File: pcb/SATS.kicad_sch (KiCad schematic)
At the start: 34 parts, among them J1 Raspberry_Pi_2_3, J10 EXT_GPIO, J11 EXT_GPIO, J12 EXT_GPIO, J13 EXT_GPIO, J2 A00-432-262-450, J3 AudioJack4_SwitchTR1, J4 5V, J5 3.3V, J6 Card LED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

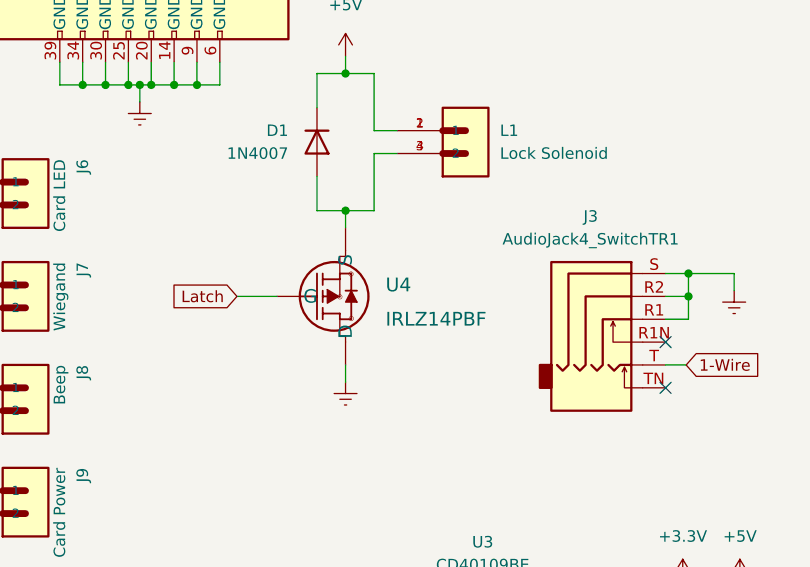
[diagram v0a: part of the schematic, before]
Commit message: Add Grounded Copper Fills to Row Breakout and Main Board
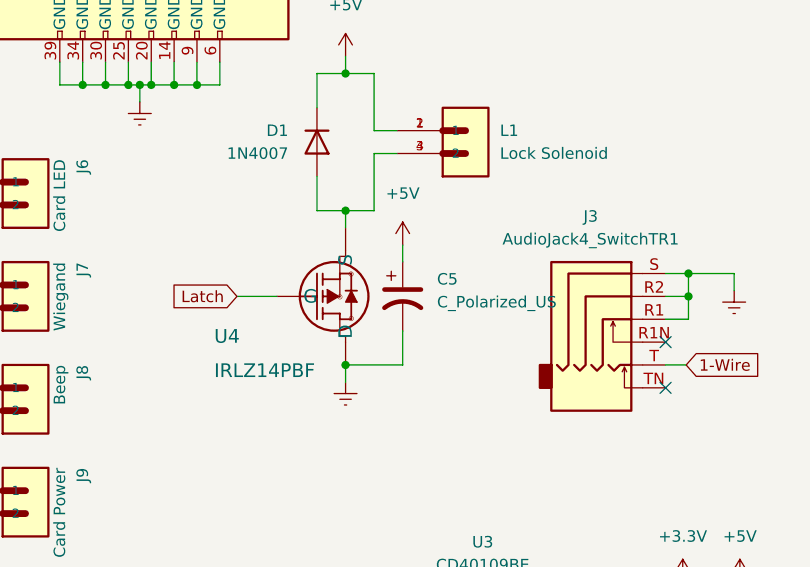
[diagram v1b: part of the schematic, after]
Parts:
- added C5: C_Polarized_US, symbol Device:C_Polarized_US
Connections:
- net +5V: now also C5.1
- net Earth: now also C5.2
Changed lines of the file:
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@@
   (junction (at 57.15 172.085) (diameter 0) (color 0 0 0 0)
   )
+  (junction (at 77.47 124.46) (diameter 0) (color 0 0 0 0)
+  )
   (junction (at 50.8 93.345) (diameter 0) (color 0 0 0 0)
   )
@@
     (stroke (width 0) (type default) (color 0 0 0 0))
   )
+  (wire (pts (xy 83.82 111.125) (xy 83.82 113.03))
+    (stroke (width 0) (type default) (color 0 0 0 0))
+  )
   (wire (pts (xy 83.185 98.425) (xy 80.645 98.425))
     (stroke (width 0) (type default) (color 0 0 0 0))
@@
     (stroke (width 0) (type default) (color 0 0 0 0))
   )
+  (wire (pts (xy 83.82 120.65) (xy 83.82 124.46))
+    (stroke (width 0) (type default) (color 0 0 0 0))
+  )
   (wire (pts (xy 50.8 21.59) (xy 50.8 24.765))
     (stroke (width 0) (type default) (color 0 0 0 0))
@@
     (stroke (width 0) (type default) (color 0 0 0 0))
   )
+  (wire (pts (xy 83.82 124.46) (xy 77.47 124.46))
+    (stroke (width 0) (type default) (color 0 0 0 0))
+  )
   (wire (pts (xy 58.42 93.345) (xy 55.88 93.345))
     (stroke (width 0) (type default) (color 0 0 0 0))
@@
     (pin "1")
   )
+  (symbol (lib_id "Device:C_Polarized_US") (at 83.82 116.84 0) (unit 1)
+    (in_bom yes) (on_board yes) (fields_autoplaced)
+    (property "Reference" "C5" (id 0) (at 87.63 114.9349 0)
+      (effects (font (size 1.27 1.27)) (justify left))
+    )
+    (property "Value" "C_Polarized_US" (id 1) (at 87.63 117.4749 0)
+      (effects (font (size 1.27 1.27)) (justify left))
+    )
+    (property "Footprint" "" (id 2) (at 83.82 116.84 0)
+      (effects (font (size 1.27 1.27)) hide)
+    )
+    (property "Datasheet" "~" (id 3) (at 83.82 116.84 0)
+      (effects (font (size 1.27 1.27)) hide)
+    )
+    (pin "1")
+    (pin "2")
+  )
   (symbol (lib_id "power:+3.3V") (at 57.15 168.275 0) (unit 1)
     (in_bom yes) (on_board yes)
@@
   )
   (symbol (lib_id "IRLZ14PBF:IRLZ14PBF") (at 69.85 116.84 0) (unit 1)
-    (in_bom yes) (on_board yes) (fields_autoplaced)
-    (property "Reference" "U4" (id 0) (at 81.915 115.57 0)
+    (in_bom yes) (on_board yes)
+    (property "Reference" "U4" (id 0) (at 62.865 121.285 0)
       (effects (font (size 1.524 1.524)) (justify left))
     )
-    (property "Value" "IRLZ14PBF" (id 1) (at 81.915 119.38 0)
+    (property "Value" "IRLZ14PBF" (id 1) (at 62.865 125.095 0)
       (effects (font (size 1.524 1.524)) (justify left))
     )
@@
     (pin "4")
   )
+  (symbol (lib_id "power:+5V") (at 83.82 111.125 0) (unit 1)
+    (in_bom yes) (on_board yes) (fields_autoplaced)
+    (property "Reference" "#PWR?" (id 0) (at 83.82 114.935 0)
+      (effects (font (size 1.27 1.27)) hide)
+    )
+    (property "Value" "+5V" (id 1) (at 83.82 105.41 0))
+    (property "Footprint" "" (id 2) (at 83.82 111.125 0)
+      (effects (font (size 1.27 1.27)) hide)
+    )
+    (property "Datasheet" "" (id 3) (at 83.82 111.125 0)
+      (effects (font (size 1.27 1.27)) hide)
+    )
+    (pin "1")
+  )
   (symbol (lib_id "power:+5V") (at 107.315 31.115 0) (mirror x) (unit 1)
     (in_bom yes) (on_board yes) (fields_autoplaced)
@@
       (reference "#PWR0141") (unit 1) (value "Earth") (footprint "")
     )
+    (path "/b2205868-ea15-4ad8-be8d-37b937090977"
+      (reference "#PWR?") (unit 1) (value "+5V") (footprint "")
+    )
     (path "/76312551-1f93-4c3b-b646-01a8c308431a"
       (reference "C1") (unit 1) (value "100nF") (footprint "Capacitor_THT:C_Rect_L7.0mm_W3.5mm_P5.00mm")
@@
       (reference "C4") (unit 1) (value "100nF") (footprint "Capacitor_THT:C_Rect_L7.0mm_W3.5mm_P5.00mm")
     )
+    (path "/48997d22-8d2f-4e8f-9ecb-f994183fe17f"
+      (reference "C5") (unit 1) (value "C_Polarized_US") (footprint "")
+    )
     (path "/10ba1107-77c4-4d57-9ffa-56a66acd4eae"

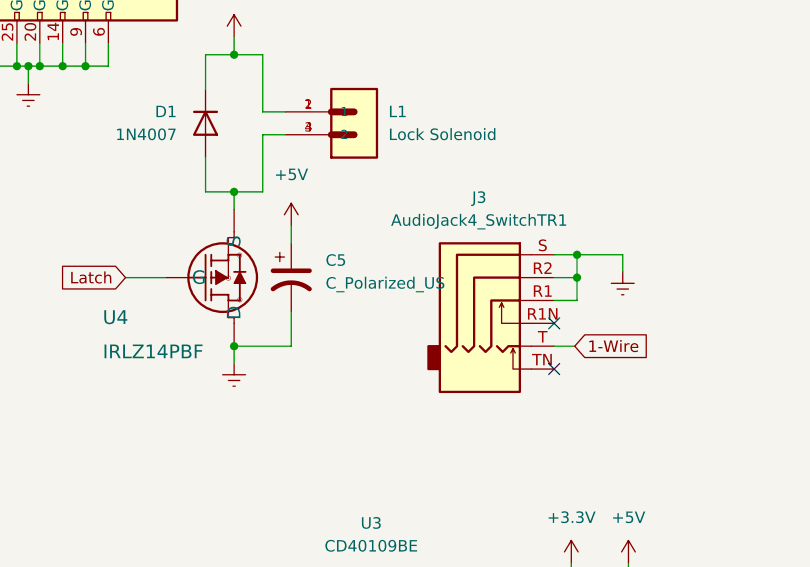
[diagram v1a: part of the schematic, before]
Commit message: Add power cap for Latch
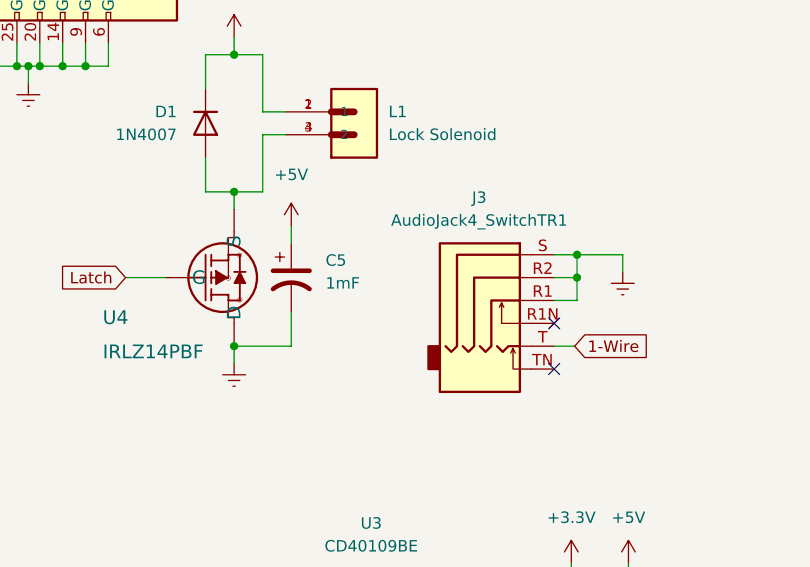
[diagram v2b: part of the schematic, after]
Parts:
- C5: value C_Polarized_US -> 1mF; footprint (none) -> Capacitor_THT:CP_Radial_D10.0mm_P5.00mm
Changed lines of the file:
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@@
       (effects (font (size 1.27 1.27)) (justify left))
     )
-    (property "Value" "C_Polarized_US" (id 1) (at 87.63 117.4749 0)
-      (effects (font (size 1.27 1.27)) (justify left))
-    )
-    (property "Footprint" "" (id 2) (at 83.82 116.84 0)
+    (property "Value" "1mF" (id 1) (at 87.63 117.4749 0)
+      (effects (font (size 1.27 1.27)) (justify left))
+    )
+    (property "Footprint" "Capacitor_THT:CP_Radial_D10.0mm_P5.00mm" (id 2) (at 83.82 116.84 0)
       (effects (font (size 1.27 1.27)) hide)
     )
@@
   (symbol (lib_id "power:+5V") (at 83.82 111.125 0) (unit 1)
     (in_bom yes) (on_board yes) (fields_autoplaced)
-    (property "Reference" "#PWR?" (id 0) (at 83.82 114.935 0)
+    (property "Reference" "#PWR0142" (id 0) (at 83.82 114.935 0)
       (effects (font (size 1.27 1.27)) hide)
     )
@@
     )
     (path "/b2205868-ea15-4ad8-be8d-37b937090977"
-      (reference "#PWR?") (unit 1) (value "+5V") (footprint "")
+      (reference "#PWR0142") (unit 1) (value "+5V") (footprint "")
     )
     (path "/76312551-1f93-4c3b-b646-01a8c308431a"
@@
     )
     (path "/48997d22-8d2f-4e8f-9ecb-f994183fe17f"
-      (reference "C5") (unit 1) (value "C_Polarized_US") (footprint "")
+      (reference "C5") (unit 1) (value "1mF") (footprint "Capacitor_THT:CP_Radial_D10.0mm_P5.00mm")
     )
     (path "/10ba1107-77c4-4d57-9ffa-56a66acd4eae"

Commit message: Rev 3 Complete
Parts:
- added R2: 10, Resistor_THT:R_Axial_DIN0207_L6.3mm_D2.5mm_P7.62mm_Horizontal, symbol Device:R_US
- renumbered R4 to R1
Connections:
- net at L1.3 (2), L1.4 (2), U4.3 (S): now also R2.2; no longer D1.2 (A)
- new net: D1.2 (A), R2.1
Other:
- moved on the sheet: C5, U4
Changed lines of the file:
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@@
   (junction (at 57.15 172.085) (diameter 0) (color 0 0 0 0)
   )
-  (junction (at 77.47 124.46) (diameter 0) (color 0 0 0 0)
+  (junction (at 77.47 133.35) (diameter 0) (color 0 0 0 0)
   )
   (junction (at 50.8 93.345) (diameter 0) (color 0 0 0 0)
   )
-  (junction (at 77.47 107.315) (diameter 0) (color 0 0 0 0)
+  (junction (at 77.47 116.205) (diameter 0) (color 0 0 0 0)
   )
   (junction (at 53.34 93.345) (diameter 0) (color 0 0 0 0)
@@
     (stroke (width 0) (type default) (color 0 0 0 0))
   )
-  (wire (pts (xy 74.295 107.315) (xy 77.47 107.315))
+  (wire (pts (xy 74.295 116.205) (xy 77.47 116.205))
     (stroke (width 0) (type default) (color 0 0 0 0))
   )
@@
     (stroke (width 0) (type default) (color 0 0 0 0))
   )
-  (wire (pts (xy 77.47 107.315) (xy 80.645 107.315))
+  (wire (pts (xy 77.47 116.205) (xy 80.645 116.205))
     (stroke (width 0) (type default) (color 0 0 0 0))
   )
@@
     (stroke (width 0) (type default) (color 0 0 0 0))
   )
+  (wire (pts (xy 74.295 113.665) (xy 74.295 116.205))
+    (stroke (width 0) (type default) (color 0 0 0 0))
+  )
   (wire (pts (xy 73.66 34.925) (xy 77.47 34.925))
     (stroke (width 0) (type default) (color 0 0 0 0))
@@
     (stroke (width 0) (type default) (color 0 0 0 0))
   )
-  (wire (pts (xy 83.82 111.125) (xy 83.82 113.03))
+  (wire (pts (xy 83.82 120.015) (xy 83.82 121.92))
     (stroke (width 0) (type default) (color 0 0 0 0))
   )
@@
     (stroke (width 0) (type default) (color 0 0 0 0))
   )
+  (wire (pts (xy 74.295 103.505) (xy 74.295 106.045))
+    (stroke (width 0) (type default) (color 0 0 0 0))
+  )
   (wire (pts (xy 160.655 133.985) (xy 158.115 133.985))
     (stroke (width 0) (type default) (color 0 0 0 0))
@@
     (stroke (width 0) (type default) (color 0 0 0 0))
   )
-  (wire (pts (xy 77.47 107.315) (xy 77.47 109.22))
+  (wire (pts (xy 77.47 116.205) (xy 77.47 118.11))
     (stroke (width 0) (type default) (color 0 0 0 0))
   )
@@
     (stroke (width 0) (type default) (color 0 0 0 0))
   )
-  (wire (pts (xy 65.405 116.84) (xy 69.85 116.84))
+  (wire (pts (xy 65.405 125.73) (xy 69.85 125.73))
     (stroke (width 0) (type default) (color 0 0 0 0))
   )
@@
     (stroke (width 0) (type default) (color 0 0 0 0))
   )
-  (wire (pts (xy 83.82 120.65) (xy 83.82 124.46))
+  (wire (pts (xy 83.82 129.54) (xy 83.82 133.35))
     (stroke (width 0) (type default) (color 0 0 0 0))
   )
@@
     (stroke (width 0) (type default) (color 0 0 0 0))
   )
-  (wire (pts (xy 83.82 124.46) (xy 77.47 124.46))
+  (wire (pts (xy 83.82 133.35) (xy 77.47 133.35))
     (stroke (width 0) (type default) (color 0 0 0 0))
   )
@@
     (stroke (width 0) (type default) (color 0 0 0 0))
   )
-  (wire (pts (xy 80.645 100.965) (xy 80.645 107.315))
+  (wire (pts (xy 80.645 100.965) (xy 80.645 116.205))
     (stroke (width 0) (type default) (color 0 0 0 0))
   )
@@
     (stroke (width 0) (type default) (color 0 0 0 0))
   )
-  (wire (pts (xy 74.295 103.505) (xy 74.295 107.315))
-    (stroke (width 0) (type default) (color 0 0 0 0))
-  )
-  (wire (pts (xy 77.47 124.46) (xy 77.47 126.365))
+  (wire (pts (xy 77.47 133.35) (xy 77.47 135.255))
     (stroke (width 0) (type default) (color 0 0 0 0))
   )
@@
     )
   )
-  (global_label "Latch" (shape input) (at 65.405 116.84 180) (fields_autoplaced)
+  (global_label "Latch" (shape input) (at 65.405 125.73 180) (fields_autoplaced)
     (effects (font (size 1.27 1.27)) (justify right))
-    (property "Intersheet References" "${INTERSHEET_REFS}" (id 0) (at 57.8514 116.7606 0)
+    (property "Intersheet References" "${INTERSHEET_REFS}" (id 0) (at 57.8514 125.6506 0)
       (effects (font (size 1.27 1.27)) (justify right) hide)
     )
@@
     (pin "1")
   )
-  (symbol (lib_id "power:Earth") (at 77.47 126.365 0) (unit 1)
+  (symbol (lib_id "Device:R_US") (at 74.295 109.855 0) (unit 1)
+    (in_bom yes) (on_board yes)
+    (property "Reference" "R2" (id 0) (at 67.31 108.585 0)
+      (effects (font (size 1.27 1.27)) (justify left))
+    )
+    (property "Value" "10" (id 1) (at 67.31 111.125 0)
+      (effects (font (size 1.27 1.27)) (justify left))
+    )
+    (property "Footprint" "Resistor_THT:R_Axial_DIN0207_L6.3mm_D2.5mm_P7.62mm_Horizontal" (id 2) (at 75.311 110.109 90)
+      (effects (font (size 1.27 1.27)) hide)
+    )
+    (property "Datasheet" "~" (id 3) (at 74.295 109.855 0)
+      (effects (font (size 1.27 1.27)) hide)
+    )
+    (pin "1")
+    (pin "2")
+  )
+  (symbol (lib_id "power:Earth") (at 77.47 135.255 0) (unit 1)
     (in_bom yes) (on_board yes) (fields_autoplaced)
-    (property "Reference" "#PWR0129" (id 0) (at 77.47 132.715 0)
+    (property "Reference" "#PWR0129" (id 0) (at 77.47 141.605 0)
       (effects (font (size 1.27 1.27)) hide)
     )
-    (property "Value" "Earth" (id 1) (at 77.47 130.175 0)
+    (property "Value" "Earth" (id 1) (at 77.47 139.065 0)
       (effects (font (size 1.27 1.27)) hide)
     )
-    (property "Footprint" "" (id 2) (at 77.47 126.365 0)
+    (property "Footprint" "" (id 2) (at 77.47 135.255 0)
       (effects (font (size 1.27 1.27)) hide)
     )
-    (property "Datasheet" "~" (id 3) (at 77.47 126.365 0)
+    (property "Datasheet" "~" (id 3) (at 77.47 135.255 0)
       (effects (font (size 1.27 1.27)) hide)
     )
@@
     (pin "1")
   )
-  (symbol (lib_id "Device:C_Polarized_US") (at 83.82 116.84 0) (unit 1)
+  (symbol (lib_id "Device:C_Polarized_US") (at 83.82 125.73 0) (unit 1)
     (in_bom yes) (on_board yes) (fields_autoplaced)
-    (property "Reference" "C5" (id 0) (at 87.63 114.9349 0)
+    (property "Reference" "C5" (id 0) (at 87.63 123.8249 0)
       (effects (font (size 1.27 1.27)) (justify left))
     )
-    (property "Value" "1mF" (id 1) (at 87.63 117.4749 0)
+    (property "Value" "1mF" (id 1) (at 87.63 126.3649 0)
       (effects (font (size 1.27 1.27)) (justify left))
     )
-    (property "Footprint" "Capacitor_THT:CP_Radial_D10.0mm_P5.00mm" (id 2) (at 83.82 116.84 0)
+    (property "Footprint" "Capacitor_THT:CP_Radial_D10.0mm_P5.00mm" (id 2) (at 83.82 125.73 0)
       (effects (font (size 1.27 1.27)) hide)
     )
-    (property "Datasheet" "~" (id 3) (at 83.82 116.84 0)
+    (property "Datasheet" "~" (id 3) (at 83.82 125.73 0)
       (effects (font (size 1.27 1.27)) hide)
     )
@@
   (symbol (lib_id "Device:R_US") (at 95.25 66.675 180) (unit 1)
     (in_bom yes) (on_board yes) (fields_autoplaced)
-    (property "Reference" "R4" (id 0) (at 97.79 65.4049 0)
+    (property "Reference" "R1" (id 0) (at 97.79 65.4049 0)
       (effects (font (size 1.27 1.27)) (justify right))
     )
@@
     (pin "2")
   )
-  (symbol (lib_id "IRLZ14PBF:IRLZ14PBF") (at 69.85 116.84 0) (unit 1)
+  (symbol (lib_id "IRLZ14PBF:IRLZ14PBF") (at 69.85 125.73 0) (unit 1)
     (in_bom yes) (on_board yes)
-    (property "Reference" "U4" (id 0) (at 62.865 121.285 0)
+    (property "Reference" "U4" (id 0) (at 62.865 130.175 0)
       (effects (font (size 1.524 1.524)) (justify left))
     )
-    (property "Value" "IRLZ14PBF" (id 1) (at 62.865 125.095 0)
+    (property "Value" "IRLZ14PBF" (id 1) (at 62.865 133.985 0)
       (effects (font (size 1.524 1.524)) (justify left))
     )
-    (property "Footprint" "Package_TO_SOT_THT:TO-220-3_Horizontal_TabDown" (id 2) (at 81.28 123.444 0)
+    (property "Footprint" "Package_TO_SOT_THT:TO-220-3_Horizontal_TabDown" (id 2) (at 81.28 132.334 0)
       (effects (font (size 1.524 1.524)) hide)
     )
-    (property "Datasheet" "" (id 3) (at 69.85 116.84 0)
+    (property "Datasheet" "" (id 3) (at 69.85 125.73 0)
       (effects (font (size 1.524 1.524)))
     )
@@
     (pin "4")
   )
-  (symbol (lib_id "power:+5V") (at 83.82 111.125 0) (unit 1)
+  (symbol (lib_id "power:+5V") (at 83.82 120.015 0) (unit 1)
     (in_bom yes) (on_board yes) (fields_autoplaced)
-    (property "Reference" "#PWR0142" (id 0) (at 83.82 114.935 0)
+    (property "Reference" "#PWR0142" (id 0) (at 83.82 123.825 0)
       (effects (font (size 1.27 1.27)) hide)
     )
-    (property "Value" "+5V" (id 1) (at 83.82 105.41 0))
-    (property "Footprint" "" (id 2) (at 83.82 111.125 0)
+    (property "Value" "+5V" (id 1) (at 83.82 114.3 0))
+    (property "Footprint" "" (id 2) (at 83.82 120.015 0)
       (effects (font (size 1.27 1.27)) hide)
     )
-    (property "Datasheet" "" (id 3) (at 83.82 111.125 0)
+    (property "Datasheet" "" (id 3) (at 83.82 120.015 0)
       (effects (font (size 1.27 1.27)) hide)
     )
@@
     )
     (path "/84da6b70-2d96-4e21-8104-32afcc256d03"
-      (reference "R4") (unit 1) (value "4.7k") (footprint "Resistor_THT:R_Axial_DIN0207_L6.3mm_D2.5mm_P7.62mm_Horizontal")
+      (reference "R1") (unit 1) (value "4.7k") (footprint "Resistor_THT:R_Axial_DIN0207_L6.3mm_D2.5mm_P7.62mm_Horizontal")
+    )
+    (path "/3ac9fd70-7920-4300-b1d6-7d56e8e9a95e"
+      (reference "R2") (unit 1) (value "10") (footprint "Resistor_THT:R_Axial_DIN0207_L6.3mm_D2.5mm_P7.62mm_Horizontal")
     )
     (path "/29c2f3c8-c017-4b12-bbcd-233a7e30b989"

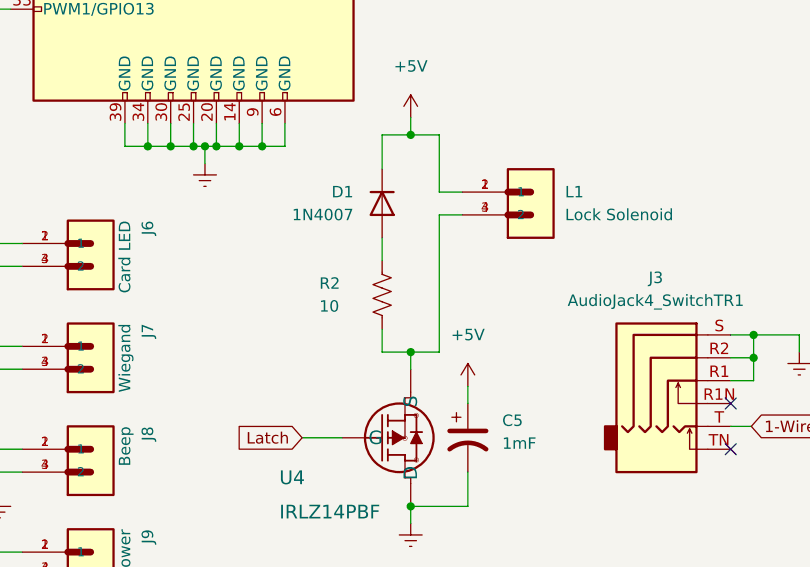
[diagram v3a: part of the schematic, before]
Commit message: Fix resistor, redate
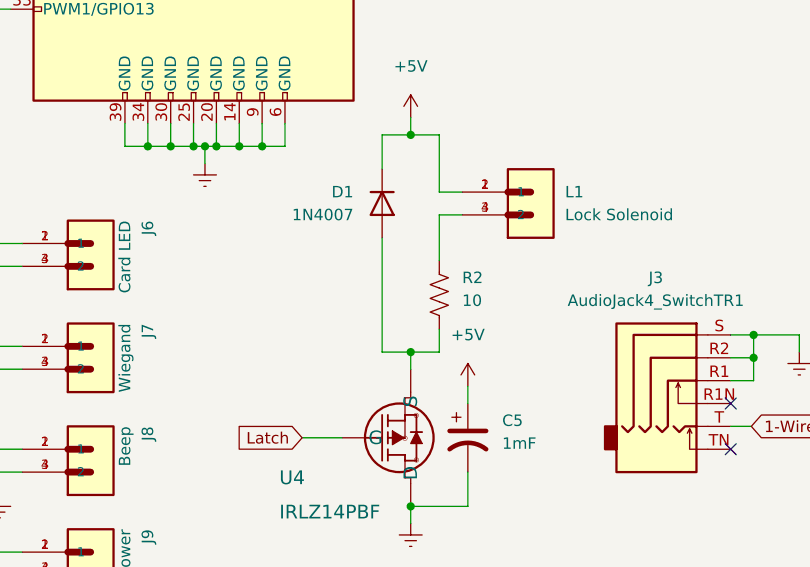
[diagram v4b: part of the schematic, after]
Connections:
- net at D1.2 (A): now also R2.2, U4.3 (S); no longer R2.1
- net at L1.3 (2), L1.4 (2): now also R2.1; no longer R2.2, U4.3 (S)
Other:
- moved on the sheet: R2

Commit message: Reev 3
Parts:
- removed H7: MountingHole, MountingHole:MountingHole_2.7mm_M2.5, symbol Mechanical:MountingHole
- added J11: SENSE Power, TerminalConn:PHOENIX_1862042, symbol TerminalConn:1862042
- J10: value EXT_GPIO -> SENSE
- renumbered J11 to J12, J12 to J13, J13 to J14
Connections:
- net +5V: now also J11.3 (2), J11.4 (2)
- net Earth: now also J11.1, J11.2 (1)
- net EXT_GPIO5 renamed TOUCH
- net EXT_GPIO6 renamed PHOTO
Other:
- moved on the sheet: J10, J12, J13, J14, J6, J7, J8, J9
